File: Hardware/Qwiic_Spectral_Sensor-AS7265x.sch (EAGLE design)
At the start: 52 parts, among them J2 Serial Interface, J5 Flash Programming, J8 PTH, U1 AS72651, U2 4MB Flash, U3 AS72652, U4 AS72653

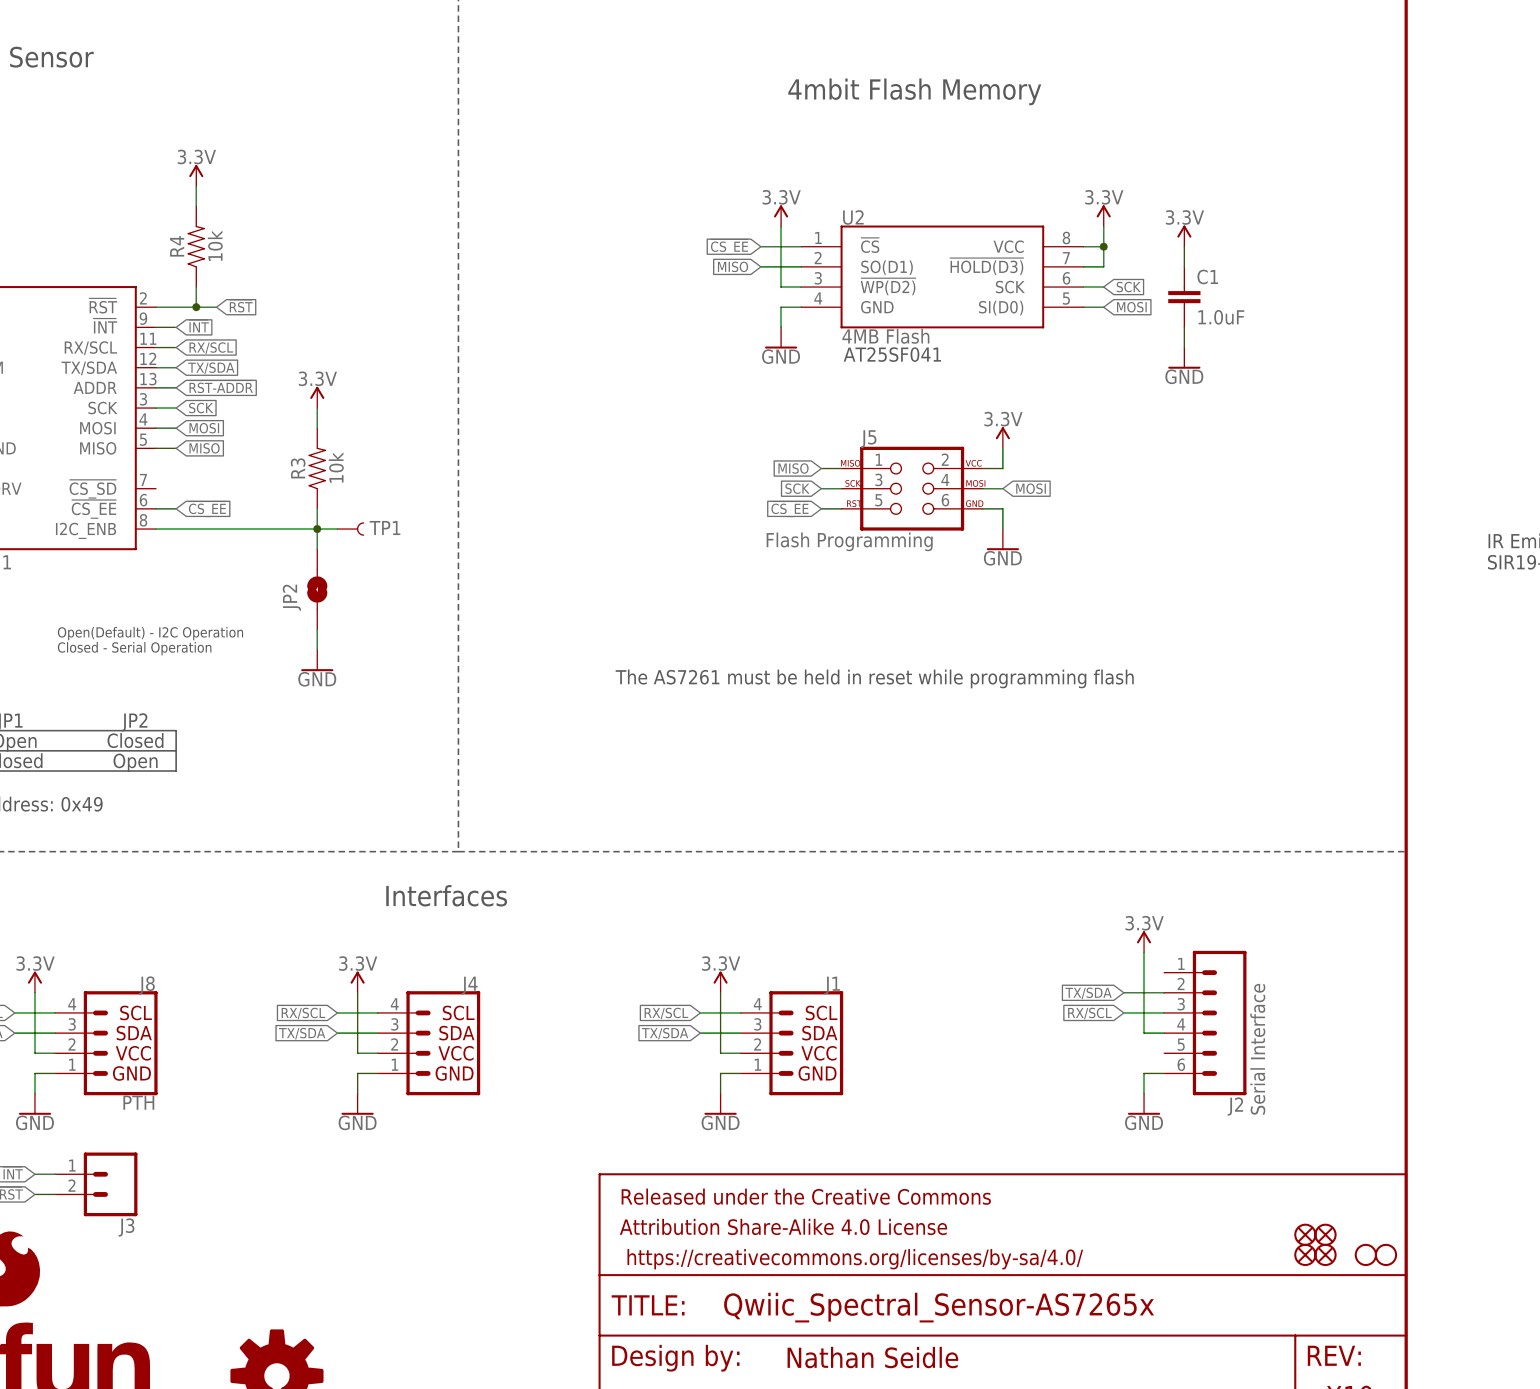
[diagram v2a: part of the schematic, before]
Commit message: Intermediate committ. Probably ignore the jig files.
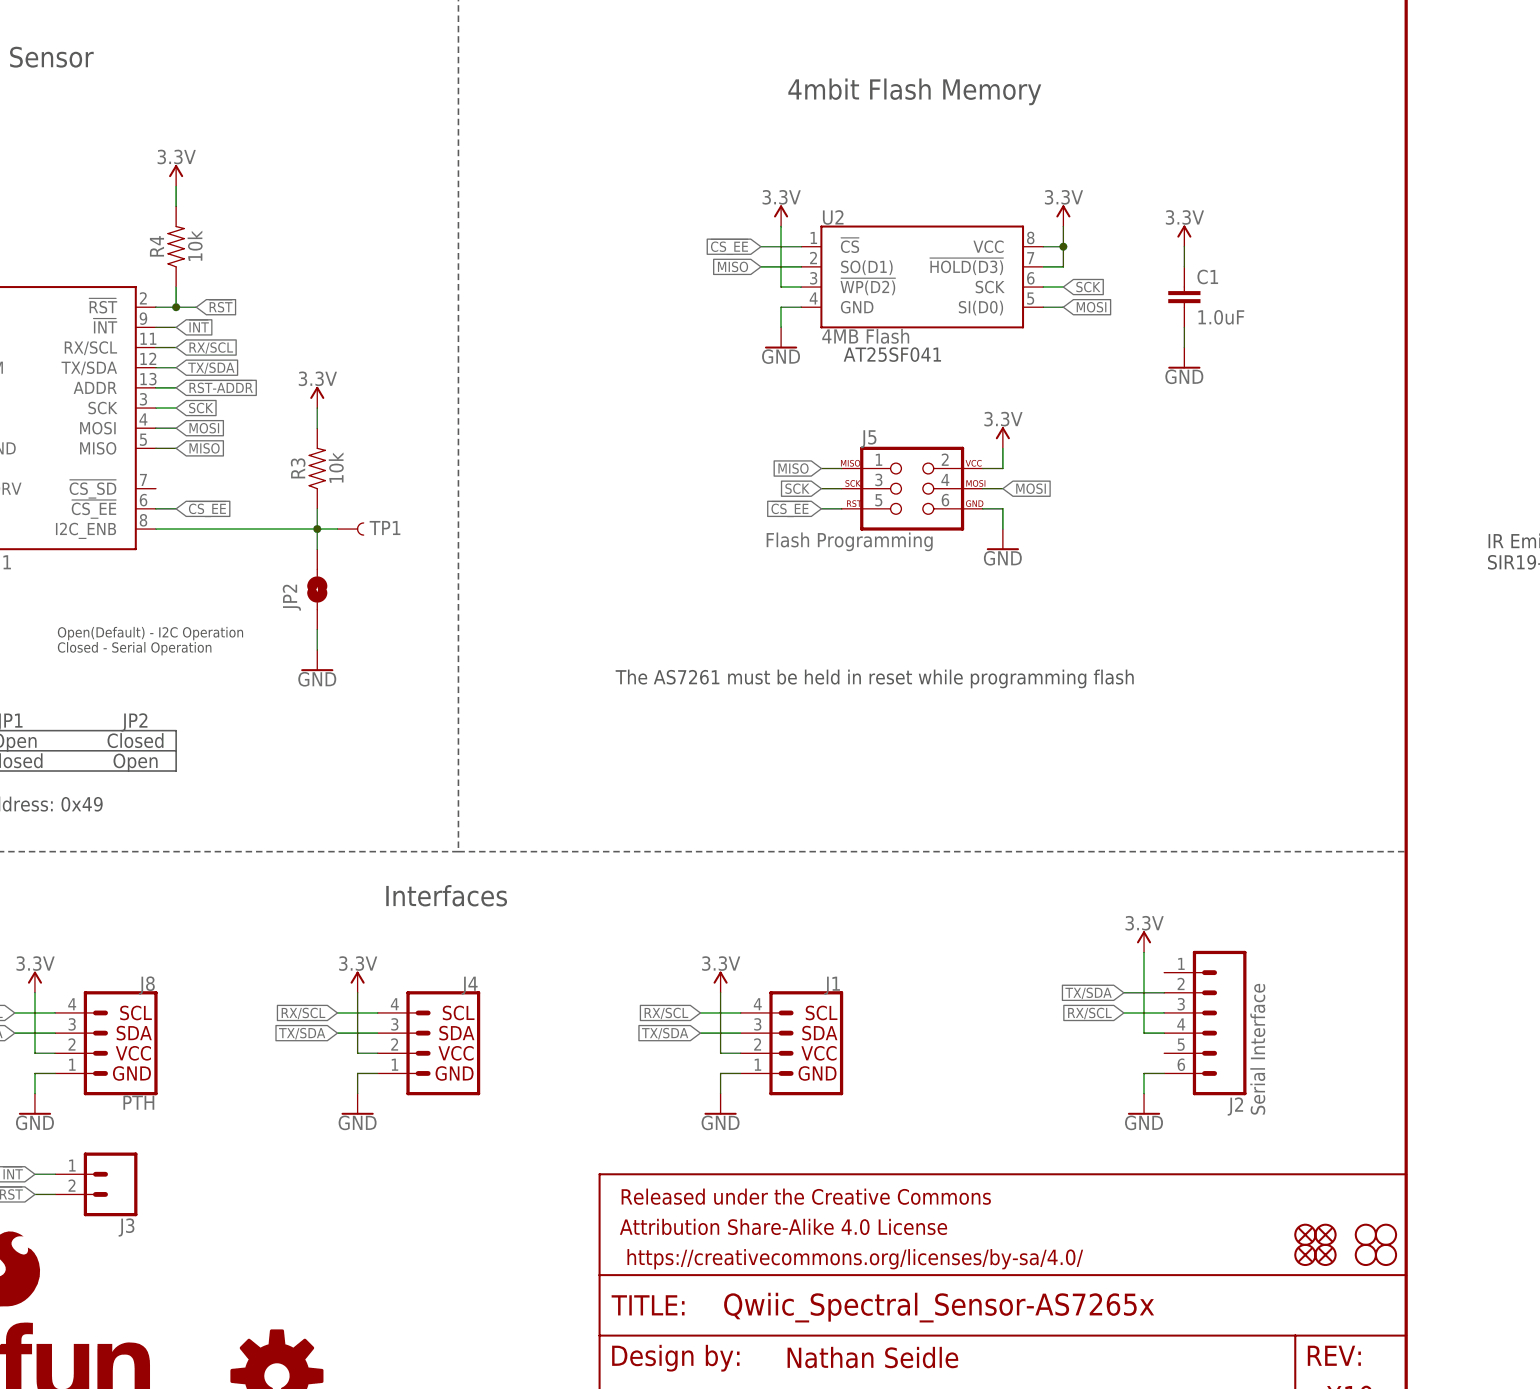
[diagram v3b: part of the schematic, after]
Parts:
- added H1, H3: STAND-OFF, SparkFun-Hardware:STAND-OFF
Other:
- moved on the sheet: R4, U2
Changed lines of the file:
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@@
 <layer number="18" name="Vias" color="2" fill="1" visible="no" active="no"/>
 <layer number="19" name="Unrouted" color="6" fill="1" visible="no" active="no"/>
-<layer number="20" name="Dimension" color="15" fill="1" visible="no" active="no"/>
+<layer number="20" name="Dimension" color="24" fill="1" visible="no" active="no"/>
 <layer number="21" name="tPlace" color="16" fill="1" visible="no" active="no"/>
 <layer number="22" name="bPlace" color="14" fill="1" visible="no" active="no"/>
@@
 <part name="TP1" library="SparkFun-Connectors" deviceset="TEST-POINT" device="3" value=""/>
 <part name="JP7" library="SparkFun-Jumpers" deviceset="JUMPER-SMT_2_NC_TRACE" device="_NO-SILK" value=""/>
+<part name="H1" library="SparkFun-Hardware" deviceset="STAND-OFF" device=""/>
+<part name="H3" library="SparkFun-Hardware" deviceset="STAND-OFF" device=""/>
 </parts>
 <sheets>
@@
 <attribute name="VALUE" x="113.284" y="124.46" size="1.778" layer="96" font="vector" rot="R90" align="top-center"/>
 </instance>
-<instance part="R4" gate="G$1" x="96.52" y="152.4" smashed="yes" rot="R90">
-<attribute name="NAME" x="94.996" y="152.4" size="1.778" layer="95" font="vector" rot="R90" align="bottom-center"/>
-<attribute name="VALUE" x="98.044" y="152.4" size="1.778" layer="96" font="vector" rot="R90" align="top-center"/>
-</instance>
-<instance part="SUPPLY4" gate="G$1" x="96.52" y="160.02" smashed="yes">
-<attribute name="VALUE" x="96.52" y="162.814" size="1.778" layer="96" align="bottom-center"/>
-</instance>
-<instance part="U2" gate="G$1" x="187.96" y="147.32" smashed="yes">
-<attribute name="NAME" x="177.8" y="155.194" size="1.778" layer="95" font="vector"/>
-<attribute name="VALUE" x="177.8" y="141.986" size="1.778" layer="96" font="vector" align="top-left"/>
+<instance part="R4" gate="G$1" x="93.98" y="152.4" smashed="yes" rot="R90">
+<attribute name="NAME" x="92.456" y="152.4" size="1.778" layer="95" font="vector" rot="R90" align="bottom-center"/>
+<attribute name="VALUE" x="95.504" y="152.4" size="1.778" layer="96" font="vector" rot="R90" align="top-center"/>
+</instance>
+<instance part="SUPPLY4" gate="G$1" x="93.98" y="160.02" smashed="yes">
+<attribute name="VALUE" x="93.98" y="162.814" size="1.778" layer="96" align="bottom-center"/>
+</instance>
+<instance part="U2" gate="G$1" x="185.42" y="147.32" smashed="yes">
+<attribute name="NAME" x="175.26" y="155.194" size="1.778" layer="95" font="vector"/>
+<attribute name="VALUE" x="175.26" y="141.986" size="1.778" layer="96" font="vector" align="top-left"/>
 </instance>
 <instance part="C1" gate="G$1" x="220.98" y="144.78" smashed="yes">
@@
 <attribute name="VALUE" x="220.98" y="136.906" size="1.778" layer="96" align="top-center"/>
 </instance>
-<instance part="SUPPLY6" gate="G$1" x="210.82" y="154.94" smashed="yes">
-<attribute name="VALUE" x="210.82" y="157.734" size="1.778" layer="96" align="bottom-center"/>
+<instance part="SUPPLY6" gate="G$1" x="205.74" y="154.94" smashed="yes">
+<attribute name="VALUE" x="205.74" y="157.734" size="1.778" layer="96" align="bottom-center"/>
 </instance>
 <instance part="GND5" gate="1" x="170.18" y="139.7" smashed="yes">
@@
 <attribute name="VALUE" x="53.34" y="55.88" size="1.778" layer="96" font="vector" rot="R90" align="top-left"/>
 </instance>
+<instance part="H1" gate="G$1" x="243.84" y="27.94" smashed="yes"/>
+<instance part="H3" gate="G$1" x="246.38" y="27.94" smashed="yes"/>
 </instances>
 <busses>
@@
 <pinref part="R4" gate="G$1" pin="2"/>
 <pinref part="SUPPLY4" gate="G$1" pin="3.3V"/>
-<wire x1="96.52" y1="160.02" x2="96.52" y2="157.48" width="0.1524" layer="91"/>
+<wire x1="93.98" y1="160.02" x2="93.98" y2="157.48" width="0.1524" layer="91"/>
 </segment>
 <segment>
@@
 <pinref part="U2" gate="G$1" pin="VCC"/>
 <pinref part="SUPPLY6" gate="G$1" pin="3.3V"/>
-<wire x1="208.28" y1="152.4" x2="210.82" y2="152.4" width="0.1524" layer="91"/>
-<wire x1="210.82" y1="152.4" x2="210.82" y2="154.94" width="0.1524" layer="91"/>
+<wire x1="203.2" y1="152.4" x2="205.74" y2="152.4" width="0.1524" layer="91"/>
+<wire x1="205.74" y1="152.4" x2="205.74" y2="154.94" width="0.1524" layer="91"/>
 <pinref part="U2" gate="G$1" pin="!HOLD(D3)"/>
-<wire x1="208.28" y1="149.86" x2="210.82" y2="149.86" width="0.1524" layer="91"/>
-<wire x1="210.82" y1="149.86" x2="210.82" y2="152.4" width="0.1524" layer="91"/>
-<junction x="210.82" y="152.4"/>
+<wire x1="203.2" y1="149.86" x2="205.74" y2="149.86" width="0.1524" layer="91"/>
+<wire x1="205.74" y1="149.86" x2="205.74" y2="152.4" width="0.1524" layer="91"/>
+<junction x="205.74" y="152.4"/>
 </segment>
 <segment>
@@
 <pinref part="U1" gate="U1" pin="!RST"/>
 <pinref part="R4" gate="G$1" pin="1"/>
-<wire x1="91.44" y1="144.78" x2="96.52" y2="144.78" width="0.1524" layer="91"/>
-<wire x1="96.52" y1="144.78" x2="96.52" y2="147.32" width="0.1524" layer="91"/>
-<wire x1="96.52" y1="144.78" x2="99.06" y2="144.78" width="0.1524" layer="91"/>
-<junction x="96.52" y="144.78"/>
-<label x="99.06" y="144.78" size="1.27" layer="95" xref="yes"/>
+<wire x1="91.44" y1="144.78" x2="93.98" y2="144.78" width="0.1524" layer="91"/>
+<wire x1="93.98" y1="144.78" x2="93.98" y2="147.32" width="0.1524" layer="91"/>
+<wire x1="93.98" y1="144.78" x2="96.52" y2="144.78" width="0.1524" layer="91"/>
+<junction x="93.98" y="144.78"/>
+<label x="96.52" y="144.78" size="1.27" layer="95" xref="yes"/>
 </segment>
 <segment>
@@
 <segment>
 <pinref part="U2" gate="G$1" pin="SI(D0)"/>
-<wire x1="208.28" y1="144.78" x2="210.82" y2="144.78" width="0.1524" layer="91"/>
-<label x="210.82" y="144.78" size="1.27" layer="95" xref="yes"/>
+<wire x1="203.2" y1="144.78" x2="205.74" y2="144.78" width="0.1524" layer="91"/>
+<label x="205.74" y="144.78" size="1.27" layer="95" xref="yes"/>
 </segment>
 <segment>
@@
 <segment>
 <pinref part="U2" gate="G$1" pin="SCK"/>
-<wire x1="208.28" y1="147.32" x2="210.82" y2="147.32" width="0.1524" layer="91"/>
-<label x="210.82" y="147.32" size="1.27" layer="95" xref="yes"/>
-</segment>
-<segment>
+<wire x1="203.2" y1="147.32" x2="205.74" y2="147.32" width="0.1524" layer="91"/>
+<label x="205.74" y="147.32" size="1.27" layer="95" xref="yes"/>
+</segment>
+<segment>

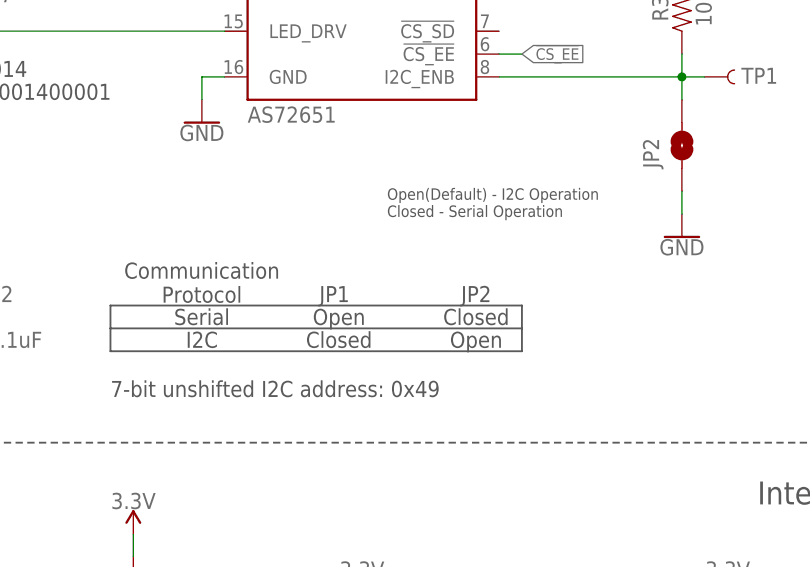
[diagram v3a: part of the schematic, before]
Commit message: Update to schematic table. Update to readme.
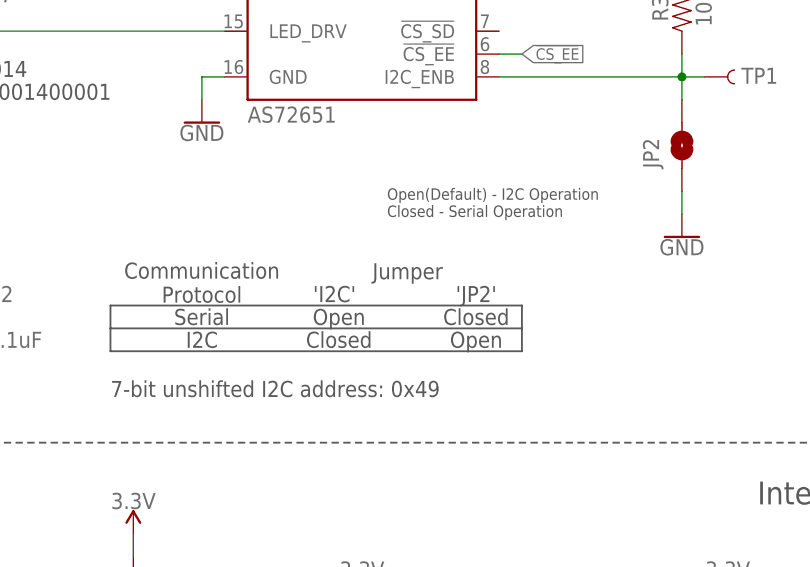
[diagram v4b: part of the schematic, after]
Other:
- note added: "'I2C'"
- note added: "'JP2'"
- note added: "Jumper"
- note removed: "JP1"
- note removed: "JP2"
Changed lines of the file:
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@@
 <text x="17.78" y="129.54" size="1.27" layer="97" rot="R90" align="center-left">Open JP4 to use an external bulb</text>
 <text x="58.42" y="90.17" size="1.778" layer="97" align="center">Serial</text>
-<text x="73.152" y="92.71" size="1.778" layer="97" align="center">JP1</text>
-<text x="88.9" y="92.71" size="1.778" layer="97" align="center">JP2</text>
+<text x="73.152" y="92.71" size="1.778" layer="97" align="center">'I2C'</text>
+<text x="88.9" y="92.71" size="1.778" layer="97" align="center">'JP2'</text>
 <text x="73.66" y="90.17" size="1.778" layer="97" align="center">Open</text>
 <text x="88.9" y="90.17" size="1.778" layer="97" align="center">Closed</text>
@@
 <text x="56.896" y="31.242" size="1.778" layer="97" rot="R90">Power Indication</text>
 <text x="178.054" y="137.922" size="1.778" layer="97">AT25SF041</text>
+<text x="81.28" y="95.25" size="1.778" layer="97" align="center">Jumper</text>
 </plain>
 <instances>

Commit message: Remvoing gerbers. Removing jig files. Rename datasheet. Clean up repo before post.
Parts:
- added FRAME3: FRAME-LETTER, SparkFun-Retired:FRAME-LETTER
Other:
- note added: "The AS72651 must be held in reset while programming flash"
- note added: "V10"
- note removed: "The AS7261 must be held in reset while programming flash"
- note removed: "X10"
